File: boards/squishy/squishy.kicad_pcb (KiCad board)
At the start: 6 copper layers, 237.4 x 150.4 mm, 169 parts, among them J1 USB_C_Receptacle, J10 QXH-060, J8 TRIGGER, J9 REFCLK, Q2 Q_NMOS_GSD, Q3 Q_NMOS_PMOS_D1G2S2D2G1S1, SW1 RST, SW2 DFU, U1 LFE5UM5G-45F-8BG381C, U10 TPS720115QDRVRQ1, U11 AD7091R-5, U12 INAx180, U13 HD3SS460, U14 TPD4E02B04DQA, U15 TPD4E02B04DQA, U16 LP5910-1.8DRVR, U17 USB3318, U2 W25N01GVZEIG, U3 CYPD3174-24, U4 SP3400-02UTG, U5 APX811-40UG-7, U6 ATSAMD09D14A-M, U7 TPS73733DRVR, U8 TPS7A1125PDRVT, U9 TPS7A1112PDRVT, X1 48MHz, X2 13MHz

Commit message: hardware: squishy: some poking around, don't quite recall what was done
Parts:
- moved C18 113.0 mm to (289.1, 185.5)
- moved C19 113.0 mm to (267.7, 197.0)
- moved C22 113.0 mm to (289.1, 184.5)
- moved C25 113.0 mm to (291.4, 183.7)
- moved C28 113.0 mm to (288.9, 187.7)
- moved C44 113.0 mm to (274.1, 171.1)
- moved R26 113.0 mm to (307.7, 213.2)
- moved TP20 113.0 mm to (272.7, 192.0)
- moved TP26 113.0 mm to (324.2, 201.3)
- moved TP28 113.0 mm to (324.2, 198.8)
- moved TP29 113.0 mm to (304.2, 196.3)
- moved C1 113.0 mm to (302.7, 188.9)
- moved C35 113.0 mm to (270.0, 194.0)
- moved C10 113.0 mm to (253.4, 200.0)
- moved C13 113.0 mm to (305.4, 201.2)
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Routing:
- net /USB Frontend/TX2-: track 3.41 -> 6.46 mm
- net /USB Frontend/TX2+: track 3.41 -> 6.46 mm
- net /USB Frontend/CC2: track 0.00 -> 0.99 mm
- net /USB Frontend/CC1: track 0.00 -> 0.81 mm, vias 0 -> 1
- net /USB Frontend/RX2-: track 3.59 -> 4.40 mm
- net /USB Frontend/RX2+: track 3.59 -> 4.40 mm
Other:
- board size 237.4 x 150.4 mm -> 313.3 x 116.1 mm
- board text added: "The spirits in this forest are older than your gods"

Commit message: hardware: squishy: got most of the USB FE done, it's a bit of a squiggly mess but should work:tm:
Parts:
- U3: moved to B.Cu
- moved U17 11.1 mm to (83.1, 164.7), turned to 90 degrees
- moved U3 2.37 mm to (90.3, 176.8)
- moved U14 1.60 mm to (81.8, 178.3)
- moved U4 1.60 mm to (82.3, 178.3)
- moved U15 1.30 mm to (84.3, 175.4)
- moved U13 1.15 mm to (83.1, 171.4)
- moved J1 0.05 mm to (83.1, 186.3)
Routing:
- net /USB Frontend/D+: track 4.36 -> 31.8 mm, vias 1 -> 3
- net /USB Frontend/D-: track 4.27 -> 31.3 mm, vias 2 -> 4
- net /USB Frontend/PLUG_POL: track 0.00 -> 14.9 mm, vias 0 -> 2
- net /USB Frontend/CC1: track 0.81 -> 11.7 mm, vias 1 -> 2
- net /USB Frontend/CC2: track 0.99 -> 11.1 mm, vias 0 -> 1
- net /USB Frontend/RX2-: track 4.40 -> 13.6 mm, vias 0 -> 2
- net /USB Frontend/RX2+: track 4.40 -> 13.5 mm, vias 0 -> 2
- net /USB Frontend/TX2-: track 6.46 -> 14.9 mm, vias 0 -> 1
- net /USB Frontend/TX2+: track 6.46 -> 14.9 mm, vias 0 -> 1
- net /USB Frontend/TX1-: track 12.6 -> 11.4 mm
- net /USB Frontend/TX1+: track 12.6 -> 11.4 mm
- net /USB Frontend/RX1-: track 13.8 -> 13.0 mm
- net /USB Frontend/RX1+: track 13.8 -> 13.0 mm
- net GND: vias 82 -> 108
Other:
- board size 313.3 x 116.1 mm -> 85 x 90 mm

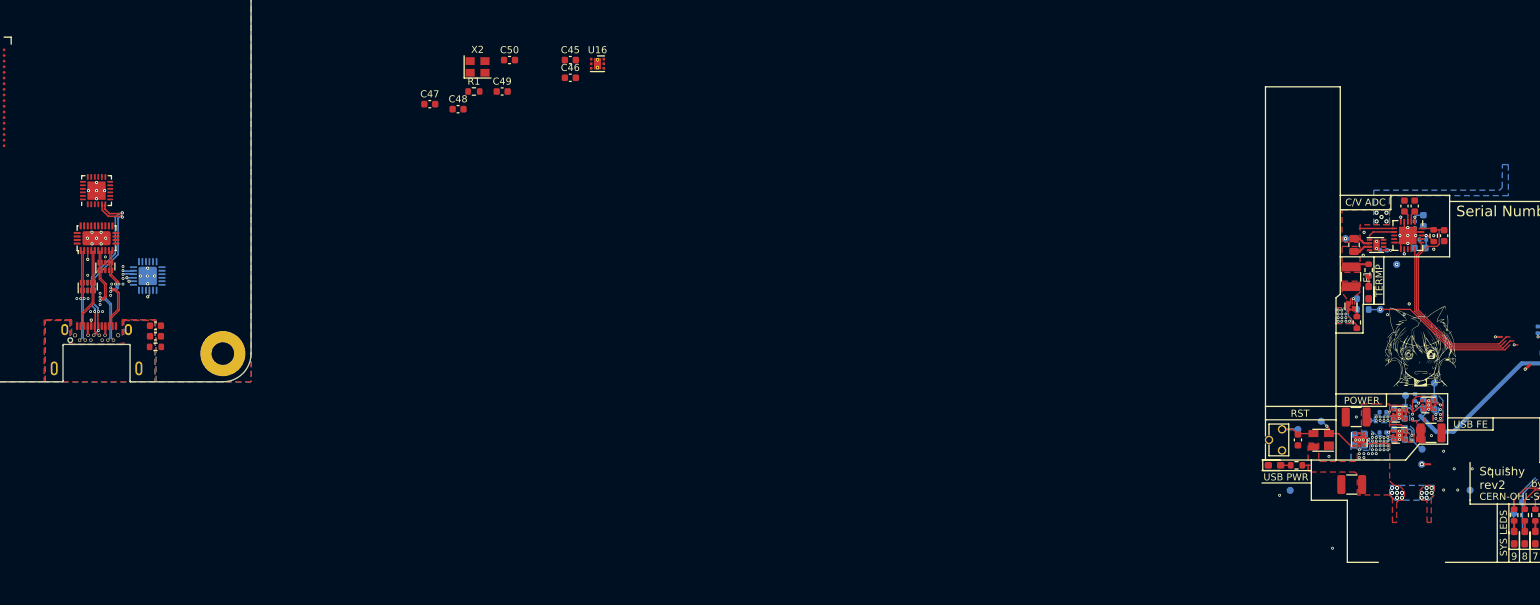
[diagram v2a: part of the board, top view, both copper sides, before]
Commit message: hardware: squishy: some more minor work on the USB FE
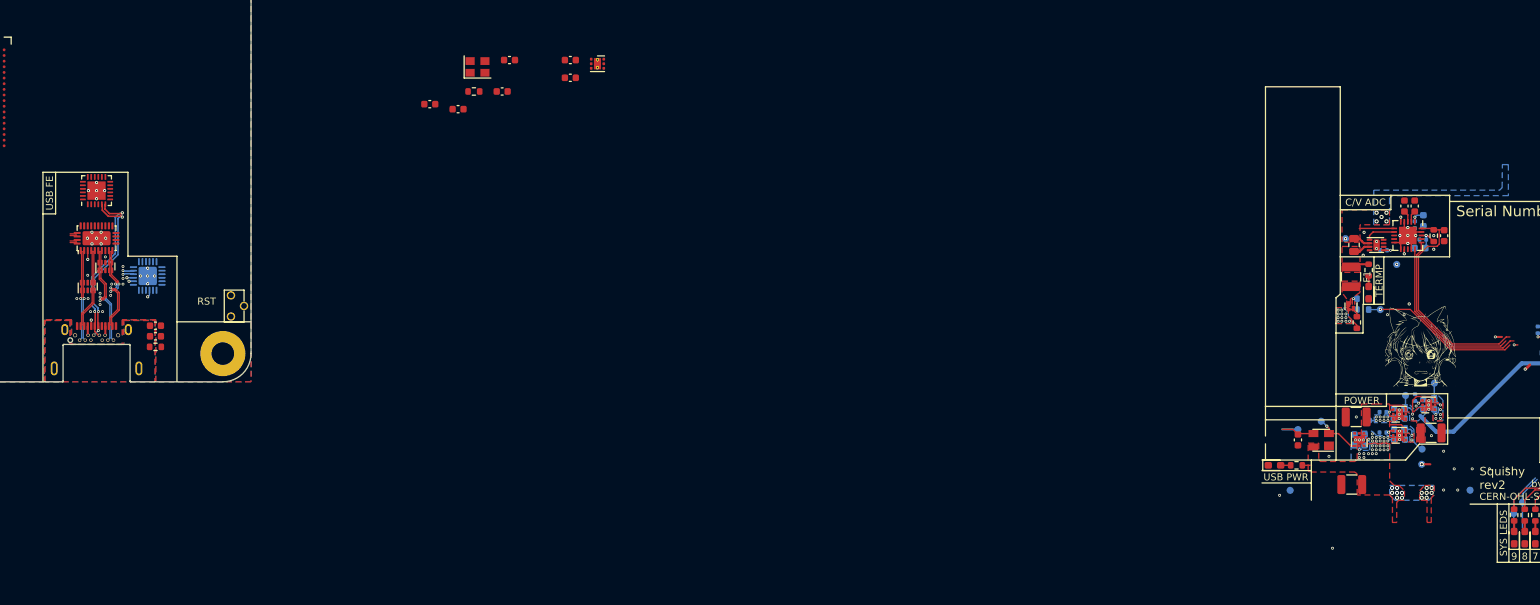
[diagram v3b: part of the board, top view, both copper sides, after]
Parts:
- moved SW1 150.2 mm to (102.2, 181.1), turned to -90 degrees
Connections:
- SW1 pad 1: GND -> Net-(C10-Pad1)
- SW1 pad 2: Net-(C10-Pad1) -> GND
- U1 pad W13: /USB Frontend/USB-FE.TX- -> unconnected-(U1-PadW13)
- U1 pad W14: /USB Frontend/USB-FE.TX+ -> unconnected-(U1-PadW14)
- U1 pad W17: unconnected-(U1-PadW17) -> /USB Frontend/USB-FE.TX-
- U1 pad W18: unconnected-(U1-PadW18) -> /USB Frontend/USB-FE.TX+
- U1 pad Y14: /USB Frontend/USB-FE.RX- -> unconnected-(U1-PadY14)
- U1 pad Y15: /USB Frontend/USB-FE.RX+ -> unconnected-(U1-PadY15)
- U1 pad Y16: unconnected-(U1-PadY16) -> /USB Frontend/USB-FE.RX-
- U1 pad Y17: unconnected-(U1-PadY17) -> /USB Frontend/USB-FE.RX+
- U3 pad 1: unconnected-(U3-Pad1) -> /USB Frontend/PLUG_PRS
- U3 pad 18: unconnected-(U3-Pad18) -> +5V
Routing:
- net /USB Frontend/USB-FE.TX-: track 0.00 -> 1.06 mm
- net /USB Frontend/USB-FE.RX-: track 0.00 -> 1.06 mm
- net /USB Frontend/USB-FE.TX+: track 0.00 -> 1.06 mm
- net /USB Frontend/USB-FE.RX+: track 0.00 -> 1.06 mm

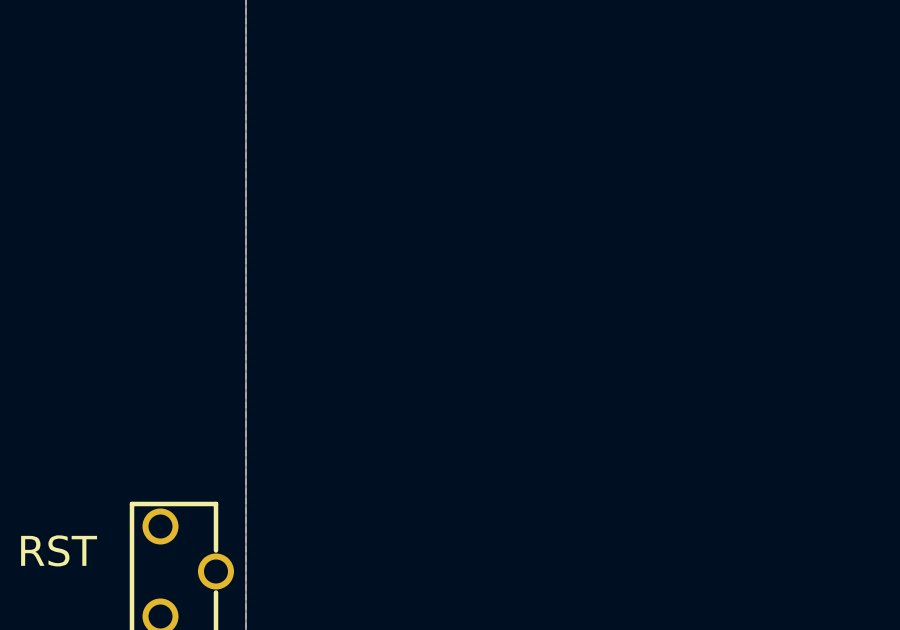
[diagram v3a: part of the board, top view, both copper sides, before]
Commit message: hardware: squishy: added the vbus resistor for the ULPI PHY
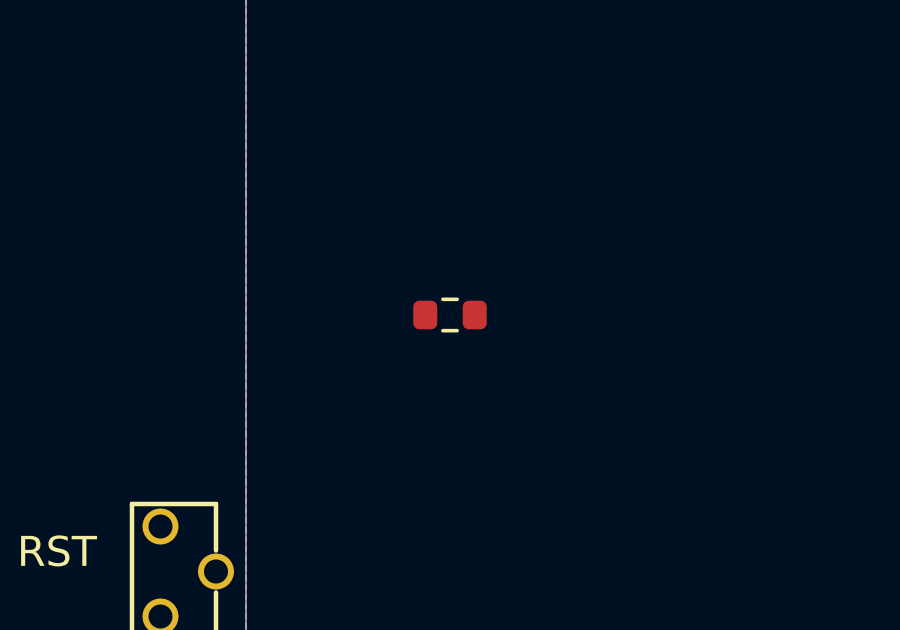
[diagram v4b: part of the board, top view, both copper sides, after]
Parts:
- added R2: 10k, Resistor_SMD:R_0603_1608Metric, F.Cu at (111.8, 172.5)
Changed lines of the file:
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@@
       (solder_mask_margin 0.375) (clearance 0.375))
+  )
+  (footprint "Resistor_SMD:R_0603_1608Metric" (layer "F.Cu")
+    (at 111.8 172.5)
+    (descr "Resistor SMD 0603 (1608 Metric), square (rectangular) end terminal, IPC_7351 nominal, (Body size source: IPC-SM-782 page 72, https://www.pcb-3d.com/wordpress/wp-content/uploads/ipc-sm-782a_amendment_1_and_2.pdf), generated with kicad-footprint-generator")
+    (tags "resistor")
+    (property "MFR" "Vishay Dale")
+    (property "MPN" "CRCW060310K0FKEA")
+    (property "Sheetfile" "squishy-usbfe.kicad_sch")
+    (property "Sheetname" "USB Frontend")
+    (attr smd)
+    (fp_text reference "R2" (at 0 -1.43) (layer "F.SilkS") hide
+      (effects (font (size 1 1) (thickness 0.15)))
+    )
+    (fp_text value "10k" (at 0 1.43) (layer "F.Fab") hide
+      (effects (font (size 1 1) (thickness 0.15)))
+    )
+    (fp_text user "${REFERENCE}" (at 0 0) (layer "F.Fab")
+      (effects (font (size 0.4 0.4) (thickness 0.06)))
+    )
+    (fp_line (start -0.237258 0.5225) (end 0.237258 0.5225) (layer "F.SilkS") (width 0.12))
+    (fp_line (start -0.237258 -0.5225) (end 0.237258 -0.5225) (layer "F.SilkS") (width 0.12))
+    (fp_line (start -1.48 -0.73) (end 1.48 -0.73) (layer "F.CrtYd") (width 0.05))
+    (fp_line (start 1.48 0.73) (end -1.48 0.73) (layer "F.CrtYd") (width 0.05))
+    (fp_line (start 1.48 -0.73) (end 1.48 0.73) (layer "F.CrtYd") (width 0.05))
+    (fp_line (start -1.48 0.73) (end -1.48 -0.73) (layer "F.CrtYd") (width 0.05))
+    (fp_line (start -0.8 0.4125) (end -0.8 -0.4125) (layer "F.Fab") (width 0.1))
+    (fp_line (start 0.8 0.4125) (end -0.8 0.4125) (layer "F.Fab") (width 0.1))
+    (fp_line (start -0.8 -0.4125) (end 0.8 -0.4125) (layer "F.Fab") (width 0.1))
+    (fp_line (start 0.8 -0.4125) (end 0.8 0.4125) (layer "F.Fab") (width 0.1))
+    (pad "1" smd roundrect (at -0.825 0) (size 0.8 0.95) (layers "F.Cu" "F.Paste" "F.Mask") (roundrect_rratio 0.25)
+      (net 485 "/USB Frontend/VBUS") (pintype "passive"))
+    (pad "2" smd roundrect (at 0.825 0) (size 0.8 0.95) (layers "F.Cu" "F.Paste" "F.Mask") (roundrect_rratio 0.25)
+      (net 2 "+5V") (pintype "passive"))
+    (model "${KICAD6_3DMODEL_DIR}/Resistor_SMD.3dshapes/R_0603_1608Metric.wrl"
+      (offset (xyz 0 0 0))
+      (scale (xyz 1 1 1))
+      (rotate (xyz 0 0 0))
+    )
   )
   (footprint "LED_SMD:LED_0603_1608Metric_Pad1.05x0.95mm_HandSolder" (layer "F.Cu")

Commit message: hardware: squishy: picking back up on things, don't recall what was updated last
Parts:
- added TP37: FP_DONE, TestPoint:TestPoint_Pad_D1.0mm, F.Cu at (144.8, 107.4)
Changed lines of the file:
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@@
     )
+  )
+  (footprint "TestPoint:TestPoint_Pad_D1.0mm" (layer "F.Cu")
+    (at 144.8 107.4)
+    (descr "SMD pad as test Point, diameter 1.0mm")
+    (tags "test point SMD pad")
+    (property "MFR" "N/A")
+    (property "MPN" "N/A")
+    (property "Sheetfile" "squishy.kicad_sch")
+    (property "Sheetname" "")
+    (attr exclude_from_pos_files)
+    (fp_text reference "TP37" (at 0 -1.448) (layer "F.SilkS") hide
+      (effects (font (size 1 1) (thickness 0.15)))
+    )
+    (fp_text value "FP_DONE" (at 0 1.55) (layer "F.Fab")
+      (effects (font (size 1 1) (thickness 0.15)))
+    )
+    (fp_text user "${REFERENCE}" (at 0 -1.45) (layer "F.Fab") hide
+      (effects (font (size 1 1) (thickness 0.15)))
+    )
+    (fp_circle (center 0 0) (end 0 0.7) (layer "F.SilkS") (width 0.12) (fill none))
+    (fp_circle (center 0 0) (end 1 0) (layer "F.CrtYd") (width 0.05) (fill none))
+    (pad "1" smd circle (at 0 0) (size 1 1) (layers "F.Cu" "F.Mask")
+      (net 34 "/FPGA_DONE") (pinfunction "1") (pintype "passive"))
   )
   (footprint "MountingHole:MountingHole_3.2mm_M3_Pad" locked (layer "F.Cu")
